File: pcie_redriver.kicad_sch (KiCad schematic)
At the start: 75 parts, among them U39 PI3EQX16904GL, U40 PI3EQX16904GL

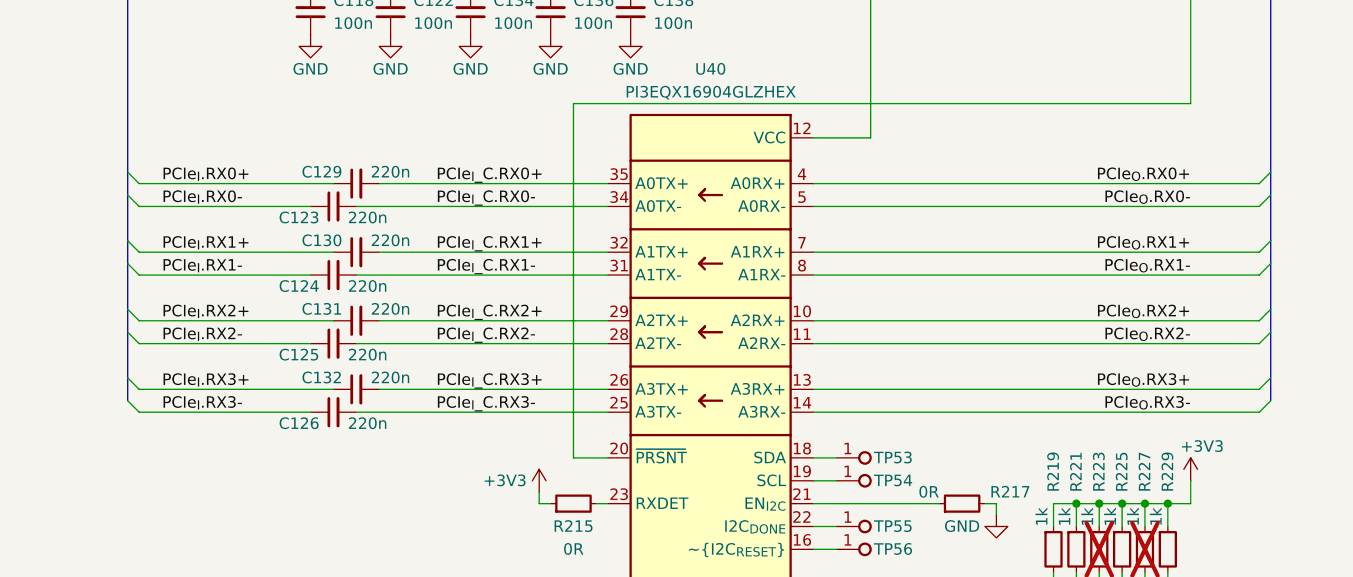
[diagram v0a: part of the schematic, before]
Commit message: [#70030] Routed PCIe
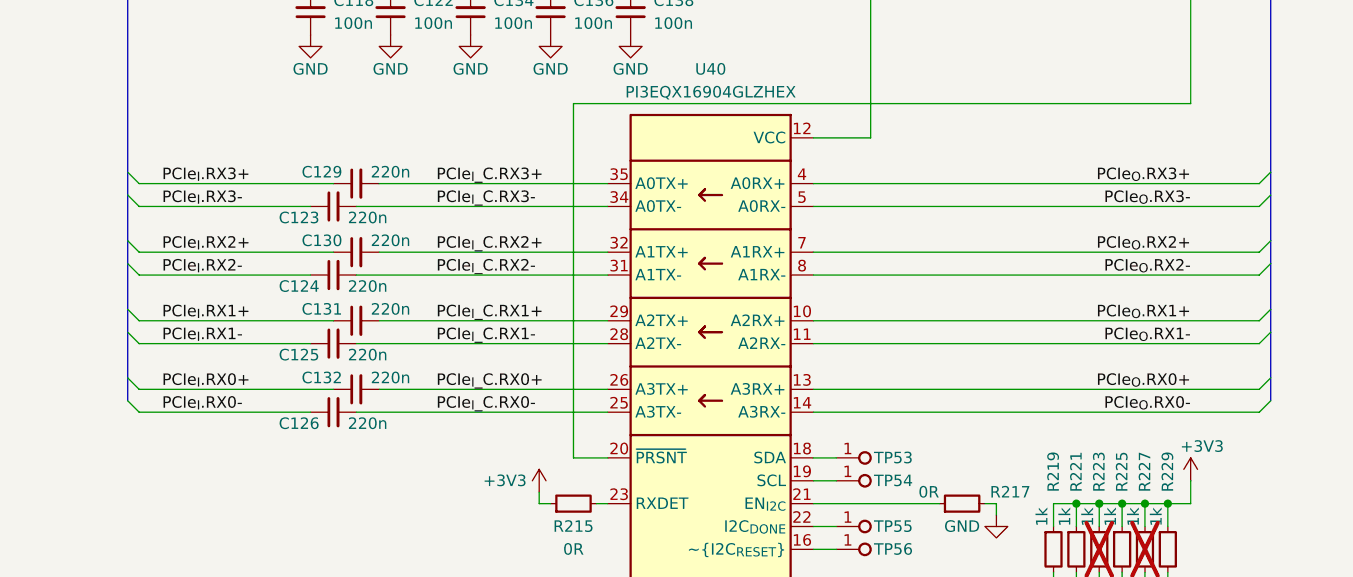
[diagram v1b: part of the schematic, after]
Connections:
- net PCIe_{I}.RX0+: now also C132.1; no longer C129.1
- net PCIe_{I}.RX0-: now also C126.1; no longer C123.1
- net PCIe_{I}.RX1+: now also C131.1; no longer C130.1
- net PCIe_{I}.RX1-: now also C125.1; no longer C124.1
- net PCIe_{I}.RX2+: now also C130.1; no longer C131.1
- net PCIe_{I}.RX2-: now also C124.1; no longer C125.1
- net PCIe_{I}.RX3+: now also C129.1; no longer C132.1
- net PCIe_{I}.RX3-: now also C123.1; no longer C126.1
- net PCIe_{I}_C.RX0+: now also C132.2, U40.26 (A3TX+); no longer C129.2, U40.35 (A0TX+)
- net PCIe_{I}_C.RX0-: now also C126.2, U40.25 (A3TX-); no longer C123.2, U40.34 (A0TX-)
- net PCIe_{I}_C.RX1+: now also C131.2, U40.29 (A2TX+); no longer C130.2, U40.32 (A1TX+)
- net PCIe_{I}_C.RX1-: now also C125.2, U40.28 (A2TX-); no longer C124.2, U40.31 (A1TX-)
- net PCIe_{I}_C.RX2+: now also C130.2, U40.32 (A1TX+); no longer C131.2, U40.29 (A2TX+)
- net PCIe_{I}_C.RX2-: now also C124.2, U40.31 (A1TX-); no longer C125.2, U40.28 (A2TX-)
- net PCIe_{I}_C.RX3+: now also C129.2, U40.35 (A0TX+); no longer C132.2, U40.26 (A3TX+)
- net PCIe_{I}_C.RX3-: now also C123.2, U40.34 (A0TX-); no longer C126.2, U40.25 (A3TX-)
- net PCIe_{O}.RX0+: now also U40.13 (A3RX+); no longer U40.4 (A0RX+)
- net PCIe_{O}.RX0-: now also U40.14 (A3RX-); no longer U40.5 (A0RX-)
- net PCIe_{O}.RX1+: now also U40.10 (A2RX+); no longer U40.7 (A1RX+)
- net PCIe_{O}.RX1-: now also U40.11 (A2RX-); no longer U40.8 (A1RX-)
- net PCIe_{O}.RX2+: now also U40.7 (A1RX+); no longer U40.10 (A2RX+)
- net PCIe_{O}.RX2-: now also U40.8 (A1RX-); no longer U40.11 (A2RX-)
- net PCIe_{O}.RX3+: now also U40.4 (A0RX+); no longer U40.13 (A3RX+)
- net PCIe_{O}.RX3-: now also U40.5 (A0RX-); no longer U40.14 (A3RX-)
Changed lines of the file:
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@@
 	)
 	(label "PCIe_{I}.RX0-"
-		(at 135.89 186.69 0)
+		(at 135.89 209.55 0)
 		(fields_autoplaced yes)
 		(effects
@@
 	)
 	(label "PCIe_{O}.RX0+"
-		(at 250.19 184.15 180)
+		(at 250.19 207.01 180)
 		(fields_autoplaced yes)
 		(effects
@@
 	)
 	(label "PCIe_{O}.RX2+"
-		(at 250.19 199.39 180)
+		(at 250.19 191.77 180)
 		(fields_autoplaced yes)
 		(effects
@@
 	)
 	(label "PCIe_{I}_C.RX1+"
-		(at 166.37 191.77 0)
+		(at 166.37 199.39 0)
 		(fields_autoplaced yes)
 		(effects
@@
 	)
 	(label "PCIe_{I}_C.RX3+"
-		(at 166.37 207.01 0)
+		(at 166.37 184.15 0)
 		(fields_autoplaced yes)
 		(effects
@@
 	)
 	(label "PCIe_{I}_C.RX2+"
-		(at 166.37 199.39 0)
+		(at 166.37 191.77 0)
 		(fields_autoplaced yes)
 		(effects
@@
 	)
 	(label "PCIe_{I}_C.RX0+"
-		(at 166.37 184.15 0)
+		(at 166.37 207.01 0)
 		(fields_autoplaced yes)
 		(effects
@@
 	)
 	(label "PCIe_{I}.RX2+"
-		(at 135.89 199.39 0)
+		(at 135.89 191.77 0)
 		(fields_autoplaced yes)
 		(effects
@@
 	)
 	(label "PCIe_{I}.RX3+"
-		(at 135.89 207.01 0)
+		(at 135.89 184.15 0)
 		(fields_autoplaced yes)
 		(effects
@@
 	)
 	(label "PCIe_{I}_C.RX0-"
+		(at 166.37 209.55 0)
+		(fields_autoplaced yes)
+		(effects
+			(font
+				(size 1.27 1.27)
+			)
+			(justify left bottom)
+		)
+	)
+	(label "PCIe_{I}_C.RX3-"
 		(at 166.37 186.69 0)
 		(fields_autoplaced yes)
@@
 		)
 	)
-	(label "PCIe_{I}_C.RX3-"
-		(at 166.37 209.55 0)
-		(fields_autoplaced yes)
-		(effects
-			(font
-				(size 1.27 1.27)
-			)
-			(justify left bottom)
-		)
-	)
 	(label "PCIe_{I}_C.RX2-"
-		(at 166.37 201.93 0)
+		(at 166.37 194.31 0)
 		(fields_autoplaced yes)
 		(effects
@@
 	)
 	(label "PCIe_{I}.RX1-"
-		(at 135.89 194.31 0)
+		(at 135.89 201.93 0)
 		(fields_autoplaced yes)
 		(effects
@@
 	)
 	(label "PCIe_{O}.RX0-"
-		(at 250.19 186.69 180)
+		(at 250.19 209.55 180)
 		(fields_autoplaced yes)
 		(effects
@@
 	)
 	(label "PCIe_{O}.RX1-"
+		(at 250.19 201.93 180)
+		(fields_autoplaced yes)
+		(effects
+			(font
+				(size 1.27 1.27)
+			)
+			(justify right bottom)
+		)
+	)
+	(label "PCIe_{O}.RX2-"
 		(at 250.19 194.31 180)
-		(fields_autoplaced yes)
-		(effects
-			(font
-				(size 1.27 1.27)
-			)
-			(justify right bottom)
-		)
-	)
-	(label "PCIe_{O}.RX2-"
-		(at 250.19 201.93 180)
 		(fields_autoplaced yes)
 		(effects
@@
 	)
 	(label "PCIe_{O}.RX1+"
-		(at 250.19 191.77 180)
+		(at 250.19 199.39 180)
 		(fields_autoplaced yes)
 		(effects
@@
 	)
 	(label "PCIe_{I}.RX3-"
-		(at 135.89 209.55 0)
+		(at 135.89 186.69 0)
 		(fields_autoplaced yes)
 		(effects
@@
 	)
 	(label "PCIe_{I}.RX1+"
-		(at 135.89 191.77 0)
+		(at 135.89 199.39 0)
 		(fields_autoplaced yes)
 		(effects
@@
 	)
 	(label "PCIe_{I}_C.RX1-"
-		(at 166.37 194.31 0)
+		(at 166.37 201.93 0)
 		(fields_autoplaced yes)
 		(effects
@@
 	)
 	(label "PCIe_{I}.RX0+"
-		(at 135.89 184.15 0)
+		(at 135.89 207.01 0)
 		(fields_autoplaced yes)
 		(effects
@@
 	)
 	(label "PCIe_{O}.RX3+"
-		(at 250.19 207.01 180)
+		(at 250.19 184.15 180)
 		(fields_autoplaced yes)
 		(effects
@@
 	)
 	(label "PCIe_{I}.RX2-"
-		(at 135.89 201.93 0)
+		(at 135.89 194.31 0)
 		(fields_autoplaced yes)
 		(effects
@@
 	)
 	(label "PCIe_{O}.RX3-"
-		(at 250.19 209.55 180)
-		(fields_autoplaced yes)
-		(effects
+		(at 250.19 186.69 180)
+		(fields_autoplaced yes)
+		(effects
